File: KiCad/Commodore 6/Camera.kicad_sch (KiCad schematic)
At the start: 4 parts, among them J5 FH12-24S-0.5SH_55_, J7 FH12-22S-0.5SH55

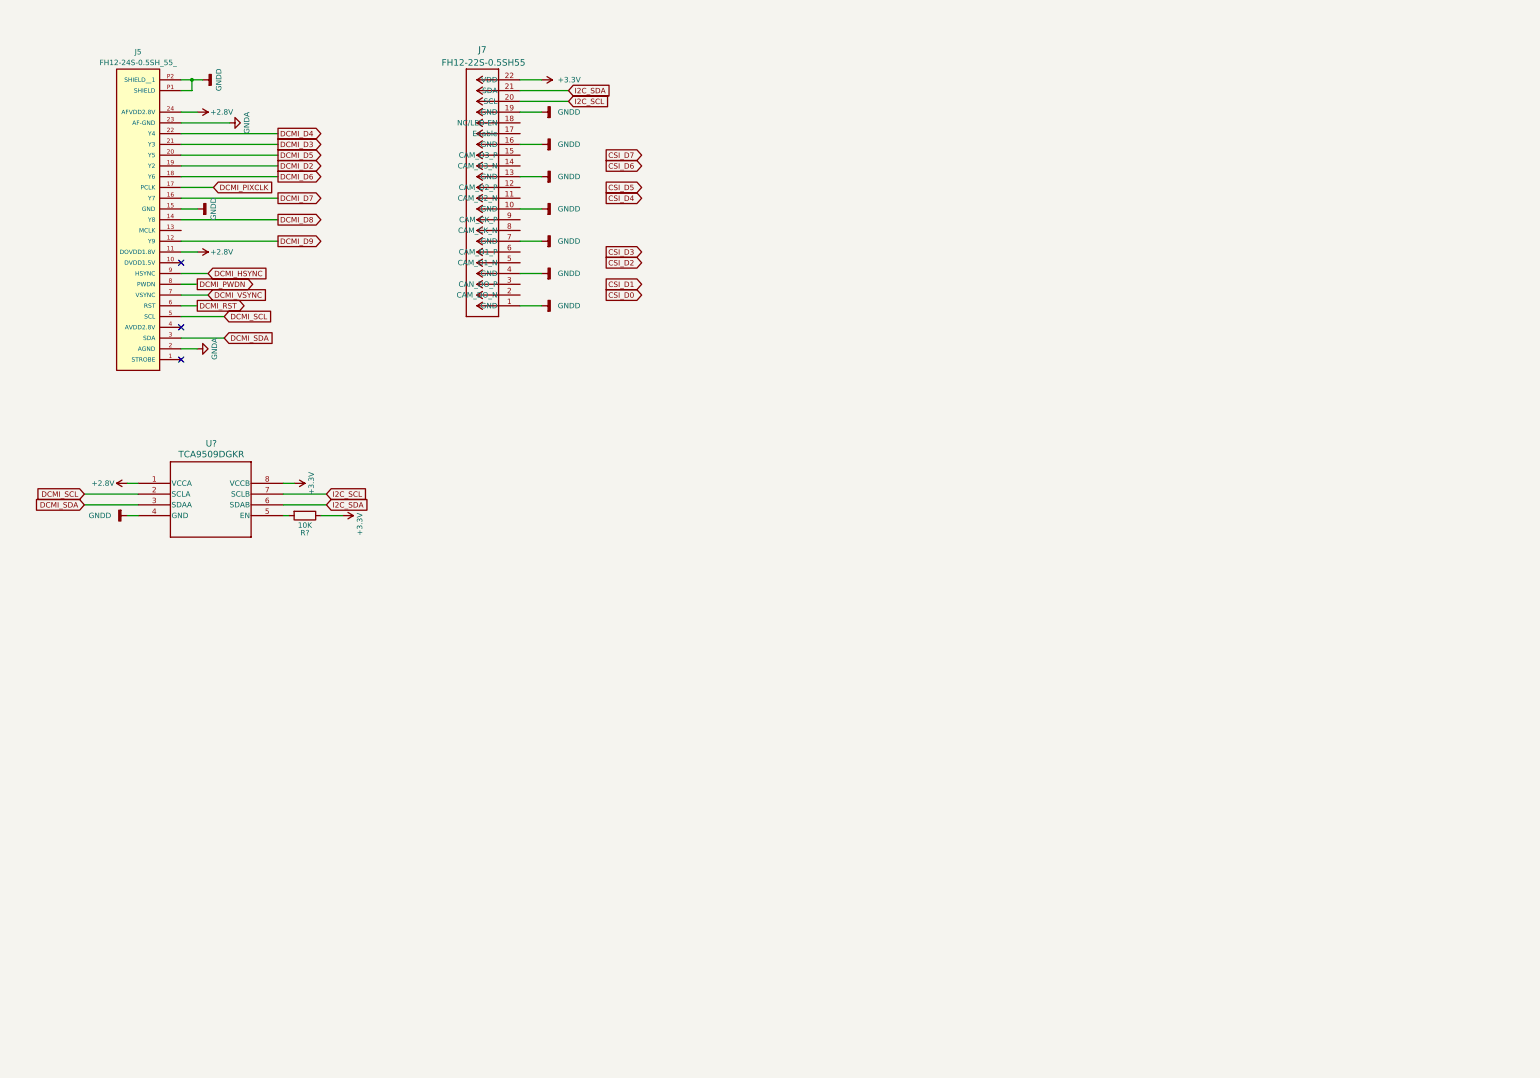
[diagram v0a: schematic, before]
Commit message: Added RunCam stuff
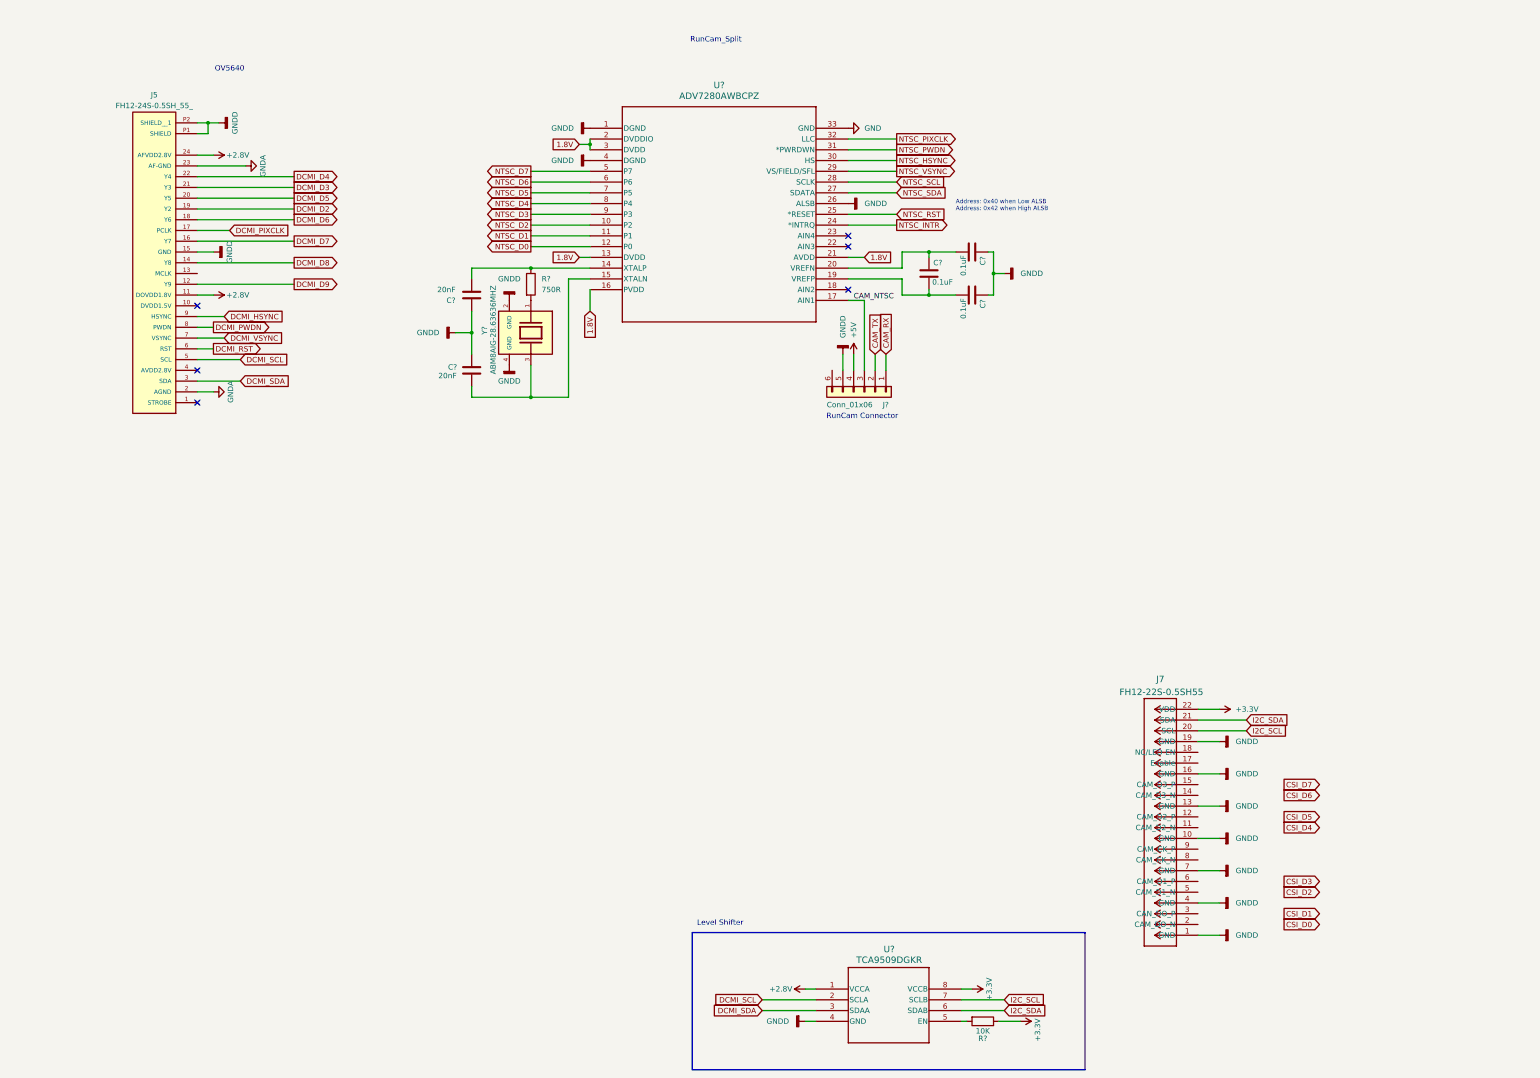
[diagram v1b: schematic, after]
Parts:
- added C? (x3): 0.1uF, symbol Device:C
- added C? (x2): 20nF, symbol Device:C
- added J?: Conn_01x06, Connector_JST:JST_XA_B06B-XASK-1_1x06_P2.50mm_Vertical, symbol Connector_Generic:Conn_01x06
- added R?: 750R, symbol Device:R
- added U?: ADV7280AWBCPZ, CP-32-12_ADI, symbol ADV7280AWBCPZ NTSC:ADV7280AWBCPZ
- added Y?: ABM8AIG-28.63636MHZ, ABM8AIG-28.63636MHZ-12-2Z-T3:XTAL_ABM8AIG-28.63636MHZ-12-2Z-T3, symbol ABM8AIG_28_63636MHZ_12_2Z_T3 Crystal:ABM8AIG-28.63636MHZ-12-2Z-T3
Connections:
- net GNDD: now also C?.1, C?.1, C?.1, C?.1, J?.5 (GND), U?.1 (DGND), U?.26 (ALSB), U?.4 (DGND), Y?.2 (GND), Y?.4 (GND)
- new net: C?.2, C?.2, U?.19 (VREFP)
- new net: C?.2, R?.1, U?.14 (XTALP)
- new net: C?.2, U?.15 (XTALN), Y?.3
- new net: C?.1, C?.2, U?.20 (VREFN)
- new net: R?.2, Y?.1
- new net +5V: J?.4 (5V)
- new net 1.8V: U?.13 (DVDD), U?.16 (PVDD), U?.2 (DVDDIO), U?.21 (AVDD), U?.3 (DVDD)
- new net CAM_NTSC: J?.3 (NTSC), U?.17 (AIN1)
- new net CAM_RX: J?.1 (RX)
- new net CAM_TX: J?.2 (TX)
- new net GND: U?.33 (GND)
- new net NTSC_D0: U?.12 (P0)
- new net NTSC_D1: U?.11 (P1)
- new net NTSC_D2: U?.10 (P2)
- new net NTSC_D3: U?.9 (P3)
- new net NTSC_D4: U?.8 (P4)
- new net NTSC_D5: U?.7 (P5)
- new net NTSC_D6: U?.6 (P6)
- new net NTSC_D7: U?.5 (P7)
- new net NTSC_HSYNC: U?.30 (HS)
- new net NTSC_INTR: U?.24 (*INTRQ)
- new net NTSC_PIXCLK: U?.32 (LLC)
- new net NTSC_PWDN: U?.31 (*PWRDWN)
- new net NTSC_RST: U?.25 (*RESET)
- new net NTSC_SCL: U?.28 (SCLK)
- new net NTSC_SDA: U?.27 (SDATA)
- new net NTSC_VSYNC: U?.29 (VS/FIELD/SFL)
- no-connect marks 3 -> 6
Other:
- note added: "Address: 0x40 when Low ALSB Address: 0x42 when High ALSB"
- note added: "Level Shifter"
- note added: "OV5640"
- note added: "RunCam Connector"
- note added: "RunCam_Split"
- moved on the sheet: J5, J7, R?, U?

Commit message: Added Multiplexer
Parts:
- added SW?: SW_Nidec_CAS-120A1, Button_Switch_SMD:Nidec_Copal_CAS-120A, symbol Switch:SW_Nidec_CAS-120A1
- added U?: SN74CBT16233DLR, DL56, symbol SN74CBT16233DLR Multiplexer:SN74CBT16233DLR
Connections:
- net +5V: now also SW?.2 (B), U?.14 (VCC), U?.43 (VCC)
- net DCMI_D2: now also U?.56 (1B1)
- net DCMI_D3: now also U?.2 (2B1)
- net DCMI_D4: now also U?.53 (3B1)
- net DCMI_D5: now also U?.5 (4B1)
- net DCMI_D6: now also U?.50 (5B1)
- net DCMI_D7: now also U?.8 (6B1)
- net DCMI_D8: now also U?.47 (7B1)
- net DCMI_D9: now also U?.11 (8B1)
- net DCMI_HSYNC: now also U?.39 (11B1)
- net DCMI_PIXCLK: now also U?.42 (9B1)
- net DCMI_PWDN: now also U?.16 (10B1)
- net DCMI_RST: now also U?.36 (13B1)
- net DCMI_SCL: now also U?.22 (14B1)
- net DCMI_SDA: now also U?.33 (15B1)
- net DCMI_VSYNC: now also U?.19 (12B1)
- net GNDD: now also SW?.3 (A), U?.13 (GND), U?.27 (TEST1), U?.28 (TEST2), U?.44 (GND)
- net NTSC_D0: now also U?.55 (1B2)
- net NTSC_D1: now also U?.3 (2B2)
- net NTSC_D2: now also U?.52 (3B2)
- net NTSC_D3: now also U?.6 (4B2)
- net NTSC_D4: now also U?.49 (5B2)
- net NTSC_D5: now also U?.9 (6B2)
- net NTSC_D6: now also U?.46 (7B2)
- net NTSC_D7: now also U?.12 (8B2)
- net NTSC_HSYNC: now also U?.38 (11B2)
- net NTSC_PIXCLK: now also U?.41 (9B2)
- net NTSC_PWDN: now also U?.17 (10B2)
- net NTSC_RST: now also U?.35 (13B2)
- net NTSC_SCL: now also U?.23 (14B2)
- net NTSC_SDA: now also U?.32 (15B2)
- net NTSC_VSYNC: now also U?.20 (12B2)
- new net: SW?.1 (C), U?.29 (SEL2), U?.30 (SEL1)
- new net CAM_D2: U?.1 (1A)
- new net CAM_D3: U?.54 (2A)
- new net CAM_D4: U?.4 (3A)
- new net CAM_D5: U?.51 (4A)
- new net CAM_D6: U?.7 (5A)
- new net CAM_D7: U?.48 (6A)
- new net CAM_D8: U?.10 (7A)
- new net CAM_D9: U?.45 (8A)
- new net CAM_HSYNC: U?.18 (11A)
- new net CAM_PIXCLK: U?.15 (9A)
- new net CAM_PWDN: U?.40 (10A)
- new net CAM_RST: U?.21 (13A)
- new net CAM_SCL: U?.34 (14A)
- new net CAM_SDA: U?.24 (15A)
- new net CAM_VSYNC: U?.37 (12A)
- no-connect marks 6 -> 9
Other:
- note added: "Multiplexer"
- note added: "USELESS TSPMO"
- moved on the sheet: C?, J5, J7, J?, R?, U?, Y?

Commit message: Fixing small error
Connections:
- net DCMI_D8 is gone; now on net DCMI_D6: J5.14 (Y8), U?.47 (7B1)
- net DCMI_D9 is gone; now on net DCMI_D7: J5.12 (Y9), U?.11 (8B1)
- net DCMI_D2: now also J5.22 (Y4), U?.53 (3B1); no longer J5.19 (Y2), U?.56 (1B1)
- net DCMI_D3: now also J5.20 (Y5), U?.5 (4B1); no longer J5.21 (Y3), U?.2 (2B1)
- net DCMI_D4: now also J5.18 (Y6), U?.50 (5B1); no longer J5.22 (Y4), U?.53 (3B1)
- net DCMI_D5: now also J5.16 (Y7), U?.8 (6B1); no longer J5.20 (Y5), U?.5 (4B1)
- net DCMI_D6: no longer J5.18 (Y6), U?.50 (5B1)
- net DCMI_D7: no longer J5.16 (Y7), U?.8 (6B1)
- new net DCMI_D0: J5.19 (Y2), U?.56 (1B1)
- new net DCMI_D1: J5.21 (Y3), U?.2 (2B1)

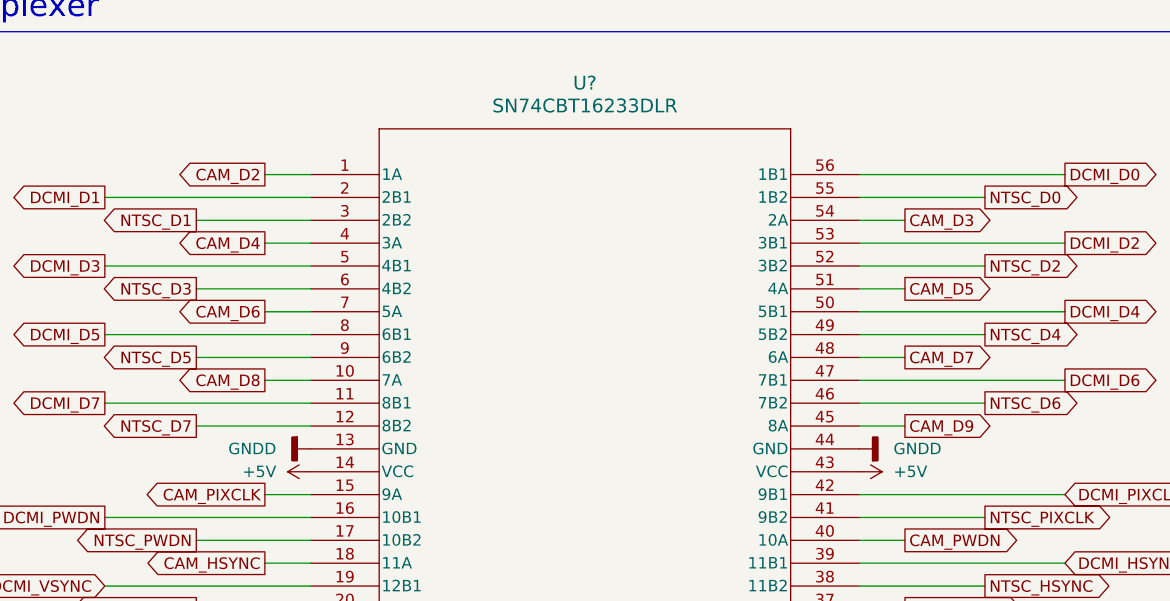
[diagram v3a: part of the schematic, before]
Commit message: Fixed Multiplexer
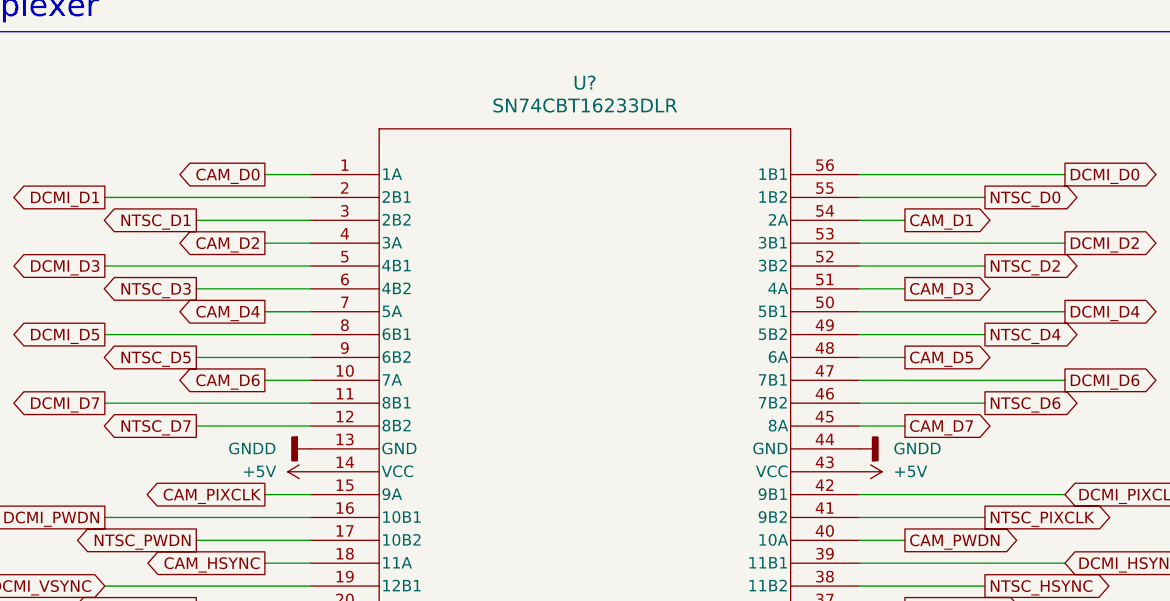
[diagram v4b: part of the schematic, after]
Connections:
- net CAM_D8 is gone; now on net CAM_D6: U?.10 (7A)
- net CAM_D9 is gone; now on net CAM_D7: U?.45 (8A)
- net CAM_D2: now also U?.4 (3A); no longer U?.1 (1A)
- net CAM_D3: now also U?.51 (4A); no longer U?.54 (2A)
- net CAM_D4: now also U?.7 (5A); no longer U?.4 (3A)
- net CAM_D5: now also U?.48 (6A); no longer U?.51 (4A)
- net CAM_D6: no longer U?.7 (5A)
- net CAM_D7: no longer U?.48 (6A)
- new net CAM_D0: U?.1 (1A)
- new net CAM_D1: U?.54 (2A)

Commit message: Small edits
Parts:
- added MK?: DMM-4026-B-I2S-R, DMM-4026-B-I2S-R:MIC_DMM-4026-B-I2S-R, symbol DMM_4026_B_I2S_R Microphone:DMM-4026-B-I2S-R
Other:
- note added: "Microphone"
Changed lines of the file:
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@@
 		)
 	)
+	(text "Microphone"
+		(exclude_from_sim no)
+		(at 160.528 206.756 0)
+		(effects
+			(font
+				(size 2.54 2.54)
+			)
+		)
+	)
 	(text "USELESS TSPMO"
 		(exclude_from_sim no)
@@
 					(unit 1)
 				)
+			)
+		)
+	)
+	(symbol
+		(lib_id "DMM_4026_B_I2S_R Microphone:DMM-4026-B-I2S-R")
+		(at 161.29 236.22 0)
+		(unit 1)
+		(exclude_from_sim no)
+		(in_bom yes)
+		(on_board yes)
+		(dnp no)
+		(fields_autoplaced yes)
+		(property "Reference" "MK?"
+			(at 161.29 220.98 0)
+			(effects
+				(font
+					(size 1.27 1.27)
+				)
+			)
+		)
+		(property "Value" "DMM-4026-B-I2S-R"
+			(at 161.29 223.52 0)
+			(effects
+				(font
+					(size 1.27 1.27)
+				)
+			)
+		)
+		(property "Footprint" "DMM-4026-B-I2S-R:MIC_DMM-4026-B-I2S-R"
+			(at 161.29 236.22 0)
+			(effects
+				(font
+					(size 1.27 1.27)
+				)
+				(justify bottom)
+				(hide yes)
+			)
+		)
+		(property "Datasheet" ""
+			(at 161.29 236.22 0)
+			(effects
+				(font
+					(size 1.27 1.27)
+				)
+				(hide yes)
+			)
+		)
+		(property "Description" ""
+			(at 161.29 236.22 0)
+			(effects
+				(font
+					(size 1.27 1.27)
+				)
+				(hide yes)
+			)
+		)
+		(property "PARTREV" "A"
+			(at 161.29 236.22 0)
+			(effects
+				(font
+					(size 1.27 1.27)
+				)
+				(justify bottom)
+				(hide yes)
+			)
+		)
+		(property "STANDARD" "Manufacturer Recommendations"
+			(at 161.29 236.22 0)
+			(effects
+				(font
+					(size 1.27 1.27)
+				)
+				(justify bottom)
+				(hide yes)
+			)
+		)
+		(property "MAXIMUM_PACKAGE_HEIGHT" "1.10 mm"
+			(at 161.29 236.22 0)
+			(effects
+				(font
+					(size 1.27 1.27)
+				)
+				(justify bottom)
+				(hide yes)
+			)
+		)
+		(property "MANUFACTURER" "PUI Audio"
+			(at 161.29 236.22 0)
+			(effects
+				(font
+					(size 1.27 1.27)
+				)
+				(justify bottom)
+				(hide yes)
+			)
+		)
+		(pin "4"
+		)
+		(pin "1"
+		)
+		(pin "5"
+		)
+		(pin "6"
+		)
+		(pin "7"
+		)
+		(pin "3"
+		)
+		(pin "2"
+		)
+		(instances
+			(project ""
+				(path "/27ad1105-577c-4f6a-be9a-9e41c9021a88/42b4c9db-c3d3-48b6-9c84-e282be31bb83/45f54d03-8d68-4556-bd65-30012701e800"
+					(reference "MK?")
+					(unit 1)
+				)

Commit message: Trying to figure out Transceiver
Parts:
- added R?: R, symbol Device:R
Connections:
- net +3.3V: now also MK?.3 (VDD)
- net GNDD: now also MK?.4 (GND), R?.2
- net at MK?.2 (CONFIG): now also R?.1
- net I2S_WS: now reaches MK?.5 (WS)
- net I2S_SCK: now reaches MK?.6 (SCK)
- net I2S_SD: now reaches MK?.7 (SD)
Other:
- moved on the sheet: J7, MK?

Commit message: P
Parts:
- added C?: 0.1uF, symbol Device:C
- added R?: 10K, symbol Device:R
- R?: value R -> 10K
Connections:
- net +3.3V: now also C?.2; no longer MK?.3 (VDD)
- net I2S_SD: now also R?.1; no longer MK?.7 (SD)
- net MIC_LR: now reaches MK?.1 (LR)
- new net: C?.1, MK?.3 (VDD)
- new net: MK?.7 (SD), R?.2
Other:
- moved on the sheet: MK?, R?
